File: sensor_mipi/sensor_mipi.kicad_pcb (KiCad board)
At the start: 4 copper layers, 44 x 77 mm, 213 parts, among them J1 SFW15R-1STE1LF, J101 DF40HC(4.0)-60DS-0.4V(51), J2 DF40C-60DP-0.4V(51), J3 <DNP> PIN1X2, J4 0878325622, J5 <DNP> SSQ-106-02-F-D-RA, U1 XC7S6-2FTGB196C, U101 NOIP1SN0300A-QTI, U102 TPS22918DBVR, U103 TPS22918DBVR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

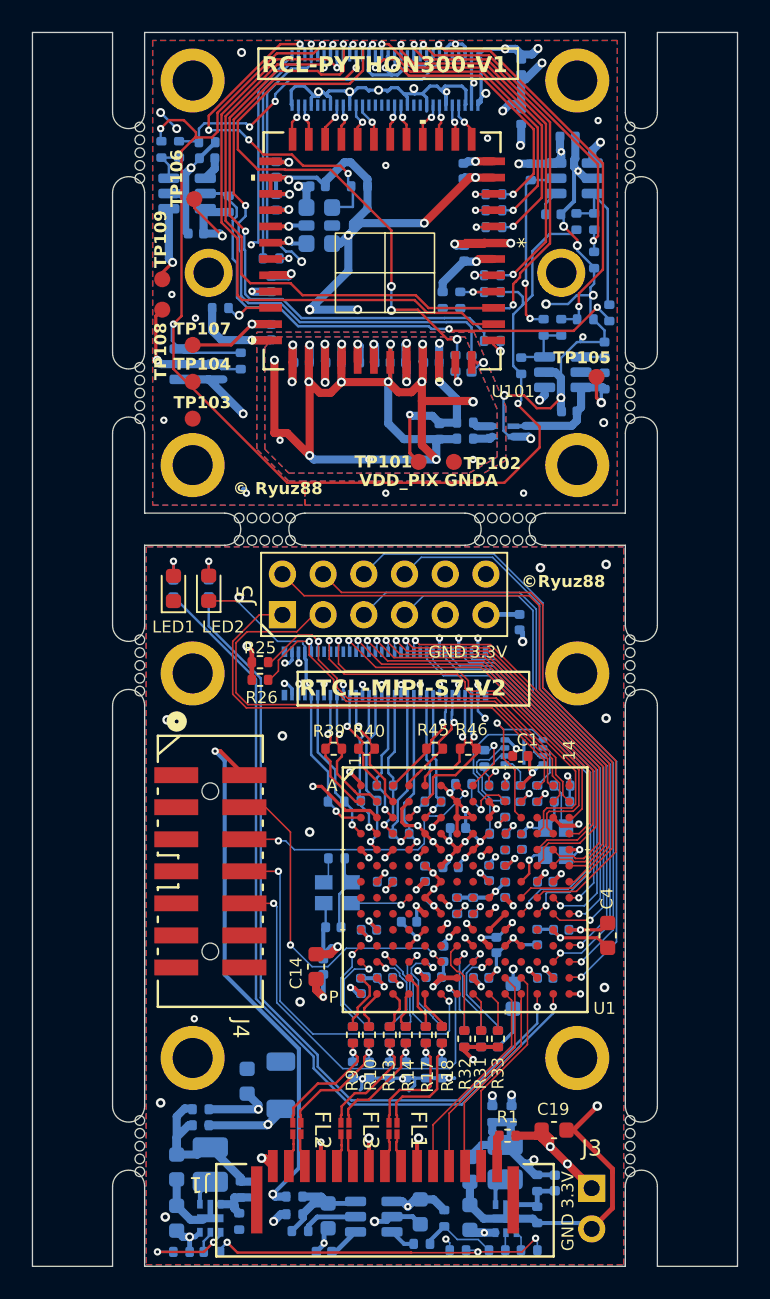
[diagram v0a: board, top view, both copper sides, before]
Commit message: 電源回路を昇圧DC-DCを使うものに変更
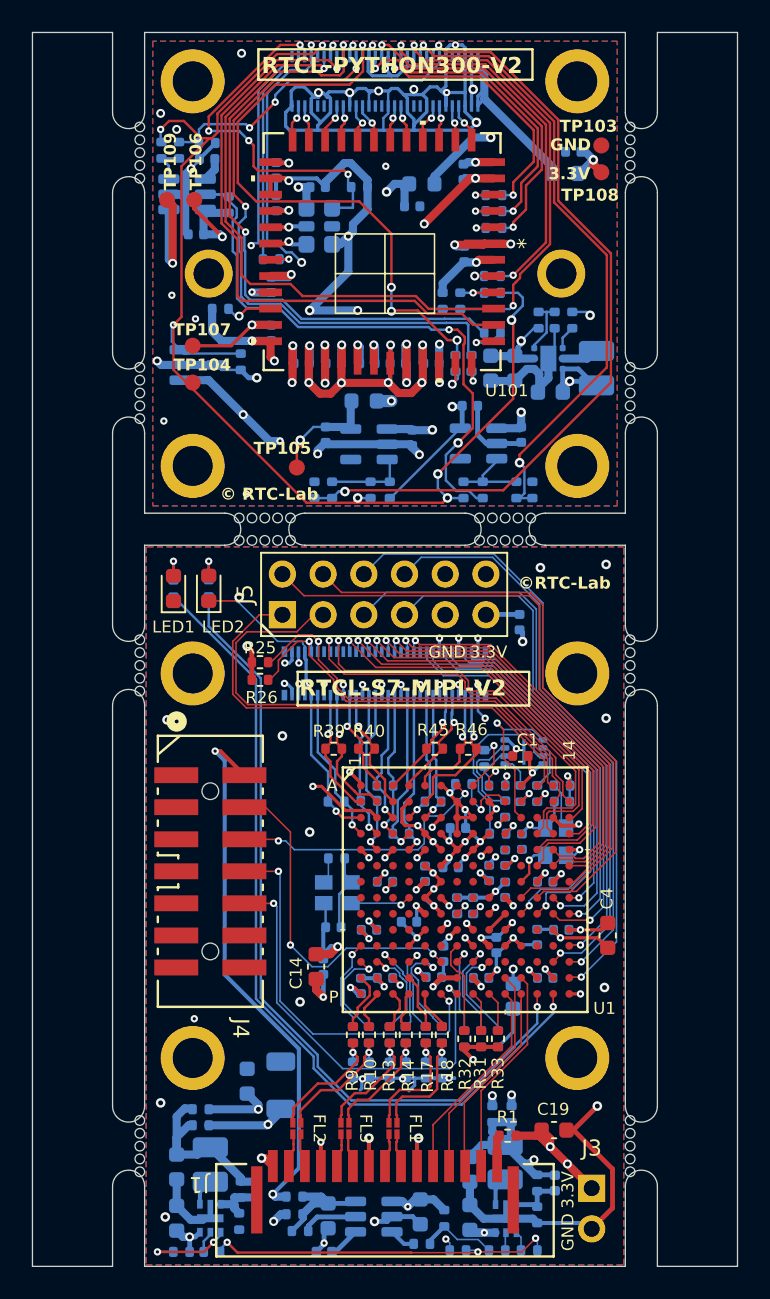
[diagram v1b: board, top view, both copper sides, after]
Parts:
- removed C115: 4.7uF, Capacitor_SMD:C_0402_1005Metric
- removed L101: EXC-24CN601X, sensor_python300:XMER_EXC-24CN601X_PAN
- removed R104: 33, Resistor_SMD:R_0402_1005Metric
- removed R105, R106: 0, Resistor_SMD:R_0402_1005Metric
- removed the REF** at (162.0, 72.0)
- removed the REF** at (138.0, 72.0)
- removed the REF** at (162.0, 96.0)
- removed the REF** at (138.0, 96.0)
- removed TP101, TP102: ~, sensor_python300:TestPin
- added C122: 10uF, Capacitor_SMD:C_0603_1608Metric, B.Cu at (160.3, 91.5)
- added C123: 10uF, Capacitor_SMD:C_0603_1608Metric, B.Cu at (156.6, 90.0)
- added C124: 10uF, Capacitor_SMD:C_0603_1608Metric, B.Cu at (158.1, 90.0)
- added FB101: BLM18AG601SN1, Inductor_SMD:L_0603_1608Metric, B.Cu at (148.7, 92.0)
- added FB102: BLM18AG601SN1, Inductor_SMD:L_0603_1608Metric, B.Cu at (161.2, 77.8)
- added FB103: BLM18AG601SN1, Inductor_SMD:L_0603_1608Metric, B.Cu at (152.3, 78.5)
- added L102: 2.2uH, Inductor_SMD:L_1008_2520Metric, B.Cu at (163.2, 90.0)
- added R131: <DNP> R, Resistor_SMD:R_0402_1005Metric, B.Cu at (159.6, 87.0)
- added R132: <DNP> R, Resistor_SMD:R_0402_1005Metric, B.Cu at (160.6, 87.0)
- added REF**: hole_M2.5, sensor_python300:hole_M2.5, F.Cu at (138.0, 96.0)
- added REF**: hole_M2.5, sensor_python300:hole_M2.5, F.Cu at (162.0, 96.0)
- added REF**: hole_M2.5, sensor_python300:hole_M2.5, F.Cu at (162.0, 72.0)
- added REF**: hole_M2.5, sensor_python300:hole_M2.5, F.Cu at (138.0, 72.0)
- added U106: TPS610995DRVR, Package_SON:WSON-6-1EP_2x2mm_P0.65mm_EP1x1.6mm, B.Cu at (160.2, 89.3)
- C101, C114: value <DNP> C -> 1uF
- C116, C117: value 4.7uF -> 1uF
- R102: value 33 -> 0
- U102, U104: value TPS22918DBVR -> TPS7A2033PDBVR; footprint Package_TO_SOT_SMD:SOT-23-6 -> Package_TO_SOT_SMD:SOT-23-5
- moved TP103 30.7 mm to (163.5, 76.0)
- moved TP108 28.7 mm to (163.5, 77.7)
- moved R111 20.0 mm to (145.6, 97.5), turned to 90 degrees
- moved TP105 19.5 mm to (144.5, 96.2)
- moved R117 18.2 mm to (154.9, 97.5)
- moved C117 17.9 mm to (155.3, 92.3)
- moved U104 17.6 mm to (155.8, 94.7)
- moved R115 17.5 mm to (146.7, 97.5), turned to 90 degrees
- moved R107 17.4 mm to (158.2, 97.5)
- moved C116 15.3 mm to (146.3, 94.1), turned to -90 degrees
- moved R120 14.9 mm to (159.2, 97.5), turned to 90 degrees
- moved R114 14.0 mm to (150.3, 97.5), turned to -90 degrees
- moved C114 13.9 mm to (158.5, 94.1), turned to -90 degrees
- moved R116 13.6 mm to (156.1, 97.5)
- moved C101 13.2 mm to (151.7, 94.3), turned to -90 degrees
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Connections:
- C101 pad 1: Net-(U102-CT) -> +3V6
- C103 pad 2: GNDA -> GND
- C104 pad 2: GNDA -> GND
- C105 pad 2: GNDA -> GND
- C106 pad 2: GNDA -> GND
- C114 pad 1: Net-(U104-CT) -> +3V6
- J101 pad 1: +3.3VP -> /CON_V33
- J101 pad 2: +1V8 -> /CON_V18
- J101 pad 31: +3.3VP -> /CON_V33
- J101 pad 32: +1V8 -> /CON_V18
- R102 pad 1: /PGOOD_PIX -> +3.3VP
- R102 pad 2: +3.3VA -> Net-(U106-EN)
- R114 pad 2: /PGOOD_VDD33 -> VDD_33
- U101 pad 32: GNDA -> GND
- U101 pad 34: GNDA -> GND
- U101 pad 37: GNDA -> GND
- U101 pad 39: GNDA -> GND
- U102 pad 1: +3.3VP -> +3V6
- U102 pad 4: Net-(U102-CT) -> unconnected-(U102-N/C-Pad4)
- U102 pad 5: /PGOOD_PIX -> +3.3VA
- U104 pad 1: +3.3VP -> +3V6
- U104 pad 4: Net-(U104-CT) -> unconnected-(U104-N/C-Pad4)
- U104 pad 5: /PGOOD_VDD33 -> VDD_33
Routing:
- net GNDA: track 99.7 -> 0.00 mm, vias 15 -> 0
- net +3.3VP: track 179.8 -> 152.7 mm, vias 14 -> 13
- net /PWR_EN_PIX: track 25.6 -> 49.5 mm
- net +3V6: track 0.00 -> 21.0 mm, vias 0 -> 3
- net /PWR_EN_VDD33: track 21.1 -> 39.3 mm
- net +1V8: track 111.1 -> 96.4 mm, vias 6 -> 5
- net VDD_33: track 69.3 -> 83.0 mm, vias 8 -> 7
- net /CON_V18: track 0.00 -> 11.5 mm, vias 0 -> 2
- net /PGOOD_VDD33: track 11.4 -> 0.00 mm, vias 2 -> 0
- net GND: track 681.0 -> 692.4 mm, vias 124 -> 120
- net /CON_V33: track 0.00 -> 11.0 mm
- net VDD_PIX: track 60.1 -> 52.7 mm
- net /PGOOD: track 82.1 -> 76.2 mm, vias 4 -> 7
- net Net-(U104-EN): track 9.77 -> 5.39 mm
- net Net-(U106-FB): track 0.00 -> 3.58 mm
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- added copper zone on In2.Cu, net +3V6
- removed copper zone on In1.Cu, net (none)
- removed copper zone on B.Cu, net GNDA
- removed copper zone on F.Cu, net GNDA
- removed copper zone on In1.Cu, net GNDA
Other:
- board text added: "RTCL-PYTHON300-V2"
- board text added: "RTCL-S7-MIPI-V2"
- board text added: "© RTC-Lab"
- board text added: "©RTC-Lab"
- board text removed: "GNDA"
- board text removed: "RCL-PYTHON300-V1"
- board text removed: "RTCL-MIPI-S7-V2"
- board text removed: "VDD_PIX"
- board text removed: "© Ryuz88"
- board text removed: "©Ryuz88"
